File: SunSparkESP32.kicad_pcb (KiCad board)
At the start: 4 copper layers, 38.1 x 58.2 mm, 54 parts, among them J1 Conn_01x02_Pin, J2 USB_C_Receptacle_USB2.0, J3 Conn_01x03_Pin, J4 Conn_01x15_Pin, J5 Conn_01x03_Pin, J6 Conn_01x15_Pin, J7 Conn_01x01_Pin, J8 Conn_01x01_Pin, Q1 IRLML6244TRPBF, Q2 IRLML6244TRPBF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

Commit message: Removed some ERC warnings -Added NC flag to non connected pins Remapped some DIOs to actual RTC GPIOs, so that external interrupts in deep sleep are possible
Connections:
- J6 pad 10: Net-(J6-Pin_10) -> /DIO1
- J6 pad 11: Net-(J6-Pin_11) -> /DIO3
- J6 pad 9: Net-(J6-Pin_9) -> /DIO2
- U3 pad 10: Net-(J6-Pin_10) -> /DIO1
- U3 pad 11: Net-(J6-Pin_9) -> /DIO2
- U3 pad 33: DIO3 -> unconnected-(U3-GPIO37-Pad33)
- U3 pad 34: DIO2 -> unconnected-(U3-GPIO38-Pad34)
- U3 pad 41: /DIO1 -> unconnected-(U3-GPIO45-Pad41)
- U3 pad 9: Net-(J6-Pin_11) -> /DIO3
- U4 pad 11: DIO3 -> /DIO3
- U4 pad 16: DIO2 -> /DIO2
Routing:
- net /DIO2: track 0.00 -> 38.8 mm, vias 0 -> 2
- net DIO3: track 34.8 -> 0.00 mm, vias 2 -> 0
- net DIO2: track 33.0 -> 0.00 mm, vias 2 -> 0
- net /DIO3: track 0.00 -> 19.9 mm, vias 0 -> 1
- net Net-(J6-Pin_10): track 18.2 -> 0.00 mm, vias 1 -> 0
- net Net-(J6-Pin_11): track 16.8 -> 0.00 mm, vias 1 -> 0
- net Net-(J6-Pin_9): track 15.3 -> 0.00 mm, vias 1 -> 0
- net /DIO1: track 26.3 -> 33.5 mm

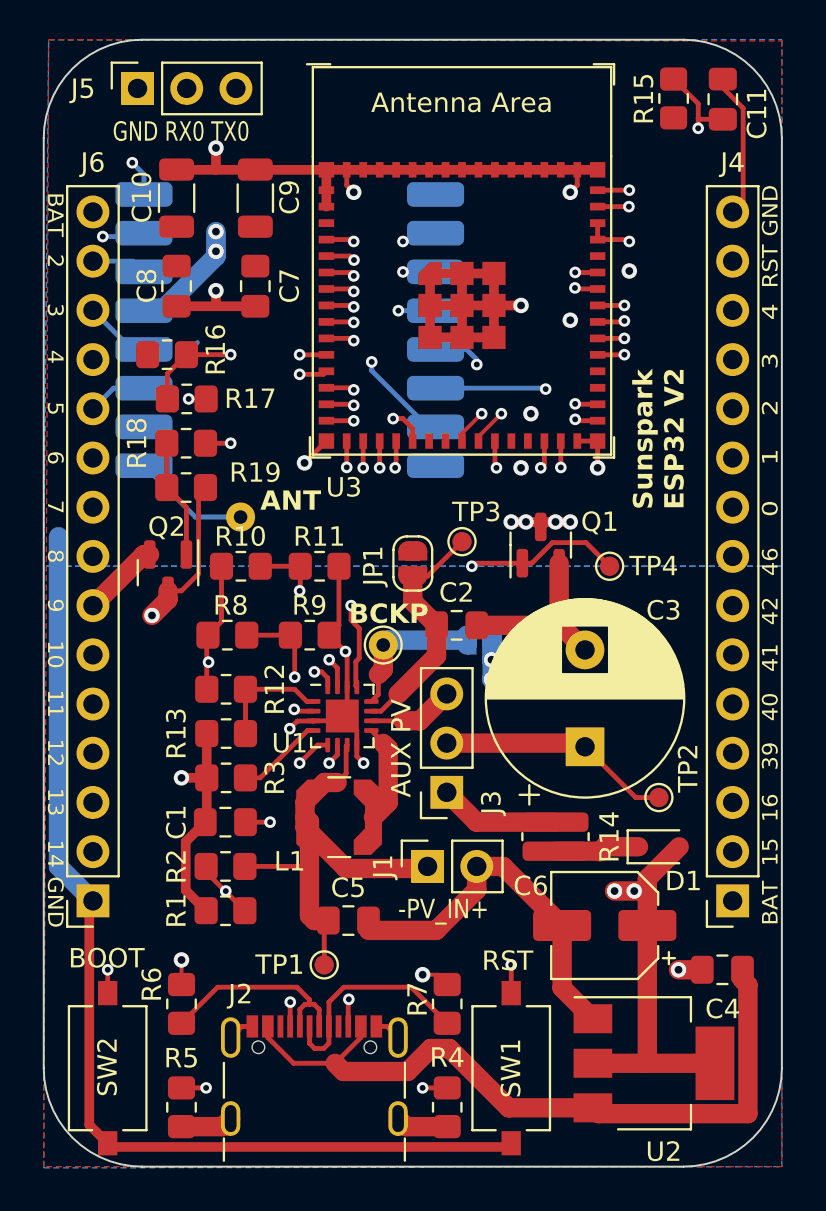
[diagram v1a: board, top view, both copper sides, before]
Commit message: Various fixes due to V2 testing -GPIO46 now not routed to external pin header -Corrected some silk -Cleaned up schematic
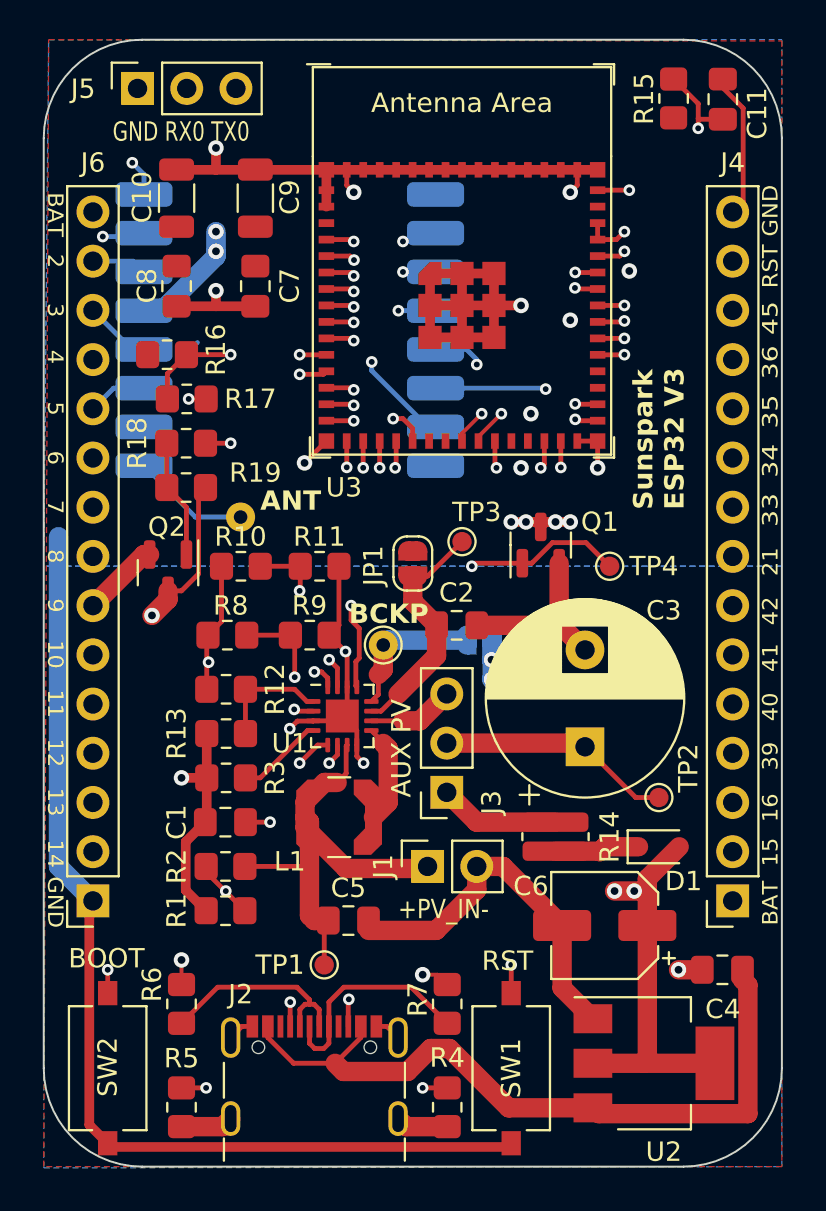
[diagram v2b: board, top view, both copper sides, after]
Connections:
- J4 pad 10: /IO1 -> /GPIO34
- J4 pad 11: /IO2 -> /GPIO35
- J4 pad 12: /IO3 -> /GPIO36
- J4 pad 13: /IO4 -> /GPIO45
- J4 pad 8: Net-(J4-Pin_8) -> /GPIO21
- J4 pad 9: /IO0 -> /GPIO33
- U3 pad 25: /IO0 -> /GPIO21
- U3 pad 28: /IO1 -> /GPIO33
- U3 pad 29: /IO2 -> /GPIO34
- U3 pad 31: /IO3 -> /GPIO35
- U3 pad 32: /IO4 -> /GPIO36
- U3 pad 41: unconnected-(U3-GPIO45-Pad41) -> /GPIO45
- U3 pad 44: Net-(J4-Pin_8) -> unconnected-(U3-GPIO46-Pad44)
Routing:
- net Net-(J4-Pin_8): track 22.8 -> 0.00 mm, vias 1 -> 0
- net /GPIO21: track 0.00 -> 15.5 mm, vias 0 -> 1
- net /IO0: track 15.0 -> 0.00 mm, vias 1 -> 0
- net /IO1: track 12.6 -> 0.00 mm, vias 1 -> 0
- net /GPIO33: track 0.00 -> 12.2 mm, vias 0 -> 1
- net /IO2: track 12.1 -> 0.00 mm, vias 1 -> 0
- net /IO4: track 11.3 -> 0.00 mm, vias 1 -> 0
- net /GPIO34: track 0.00 -> 11.1 mm, vias 0 -> 1
- net /IO3: track 10.6 -> 0.00 mm, vias 1 -> 0
- net /GPIO36: track 0.00 -> 10.2 mm, vias 0 -> 1
- net /GPIO35: track 0.00 -> 9.54 mm, vias 0 -> 1
- net /GPIO45: track 0.00 -> 8.33 mm, vias 0 -> 1
- net rst_btn: track 82.3 -> 81.2 mm
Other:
- board text added: "+PV_IN-"
- board text added: "21"
- board text added: "33"
- board text added: "34"
- board text added: "35"
- board text added: "36"
- board text added: "45"
- board text added: "Sunspark ESP32 V3"
- board text removed: "-PV_IN+"
- board text removed: "0"
- board text removed: "1"
- board text removed: "46"
- board text removed: "Sunspark ESP32 V2"

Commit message: Removed some debugging connectors -Directly connected backup supply -Removed series connector to supercap
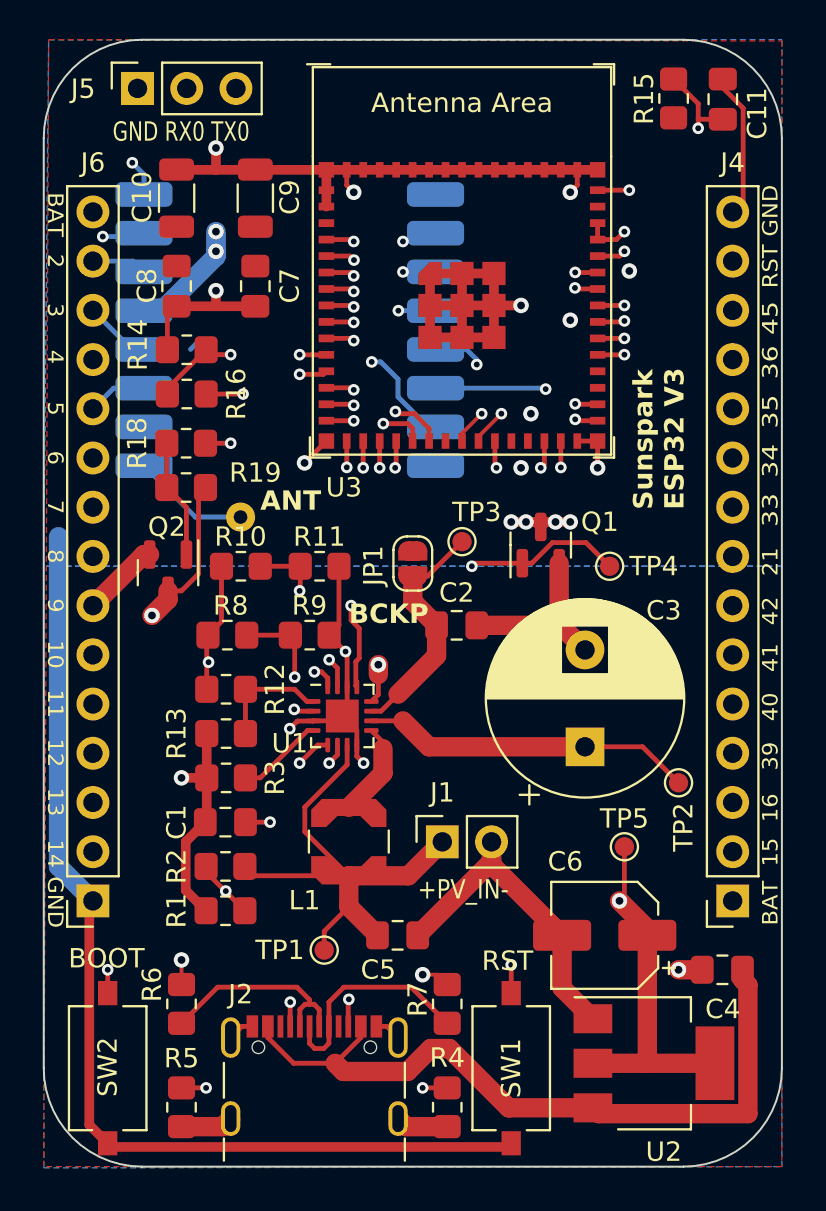
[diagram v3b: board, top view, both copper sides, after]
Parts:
- removed D1: D_Schottky, Diode_SMD:D_SOD-323
- removed J3: Conn_01x03_Pin, Connector_PinSocket_2.54mm:PinSocket_1x03_P2.54mm_Vertical
- removed J8: Conn_01x01_Pin, TestPoint:TestPoint_THTPad_D1.5mm_Drill0.7mm
- removed JP2: SolderJumper_2_Open, Jumper:SolderJumper-2_P1.3mm_Open_RoundedPad1.0x1.5mm
- removed R17: 13M, Resistor_SMD:R_0805_2012Metric_Pad1.20x1.40mm_HandSolder
- added TP5: TestPoint, TestPoint:TestPoint_Pad_D1.0mm, F.Cu at (82.0, 81.0)
- R14: value 6R8 -> 20k; footprint Resistor_SMD:R_0612_1632Metric -> Resistor_SMD:R_0805_2012Metric_Pad1.20x1.40mm_HandSolder
- R16: value 1.4M -> 20k
- moved R14 31.5 mm to (59.5, 55.4), turned to 180 degrees
- moved C5 2.65 mm to (70.3, 85.6)
- moved R16 2.27 mm to (59.5, 57.7), turned to 180 degrees
- moved J1 1.48 mm to (72.6, 80.8)
- moved L1 1.35 mm to (67.8, 80.8), turned to 90 degrees
- moved TP2 1.27 mm to (84.8, 77.7)
- moved TP1 0.76 mm to (66.5, 86.4)
- moved C6 0.51 mm to (81.0, 85.6)
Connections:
- C3 pad 1: Net-(J3-Pin_2) -> Net-(U1-BAT)
- C6 pad 1: Net-(D1-A) -> BCKP
- R14 pad 1: Net-(D1-K) -> ADC_BAT
- R14 pad 2: V_AUX -> GND1
- R16 pad 1: +BATT -> R_DIV_SUPPLY
- TP2 pad 1: Net-(J3-Pin_2) -> Net-(U1-BAT)
- U1 pad 10: Net-(J3-Pin_3) -> Net-(U1-BAT)
- U2 pad 2: Net-(D1-A) -> BCKP
- U3 pad 21: unconnected-(U3-ADC2_CH7/DAC_2/GPIO17-Pad21) -> R_DIV_SUPPLY
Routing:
- net Net-(D1-A): track 37.6 -> 0.00 mm, vias 4 -> 0
- net BCKP: track 7.59 -> 37.8 mm, vias 0 -> 2
- net R_DIV_SUPPLY: track 0.00 -> 19.5 mm, vias 0 -> 2
- net Net-(U1-BAT): track 0.00 -> 17.2 mm
- net Net-(J3-Pin_2): track 12.1 -> 0.00 mm
- net V_AUX: track 6.25 -> 0.00 mm
- net Net-(J3-Pin_3): track 4.47 -> 0.00 mm
- net Net-(D1-K): track 4.40 -> 0.00 mm
- net Net-(J4-Pin_2): track 31.3 -> 28.4 mm
- net rst_btn: track 81.2 -> 83.1 mm
- net GND1: track 125.6 -> 127.1 mm, vias 13 -> 12
- net Net-(J1-Pin_1): track 24.7 -> 26.2 mm
- net GND: track 71.2 -> 70.2 mm
- net Net-(J4-Pin_3): track 30.8 -> 31.6 mm
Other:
- board text removed: "AUX PV"
